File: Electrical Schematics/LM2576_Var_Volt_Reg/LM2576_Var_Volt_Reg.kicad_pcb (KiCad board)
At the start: 2 copper layers, 4 parts, among them J1 Conn_01x03_Pin, U1 LM2576S-12

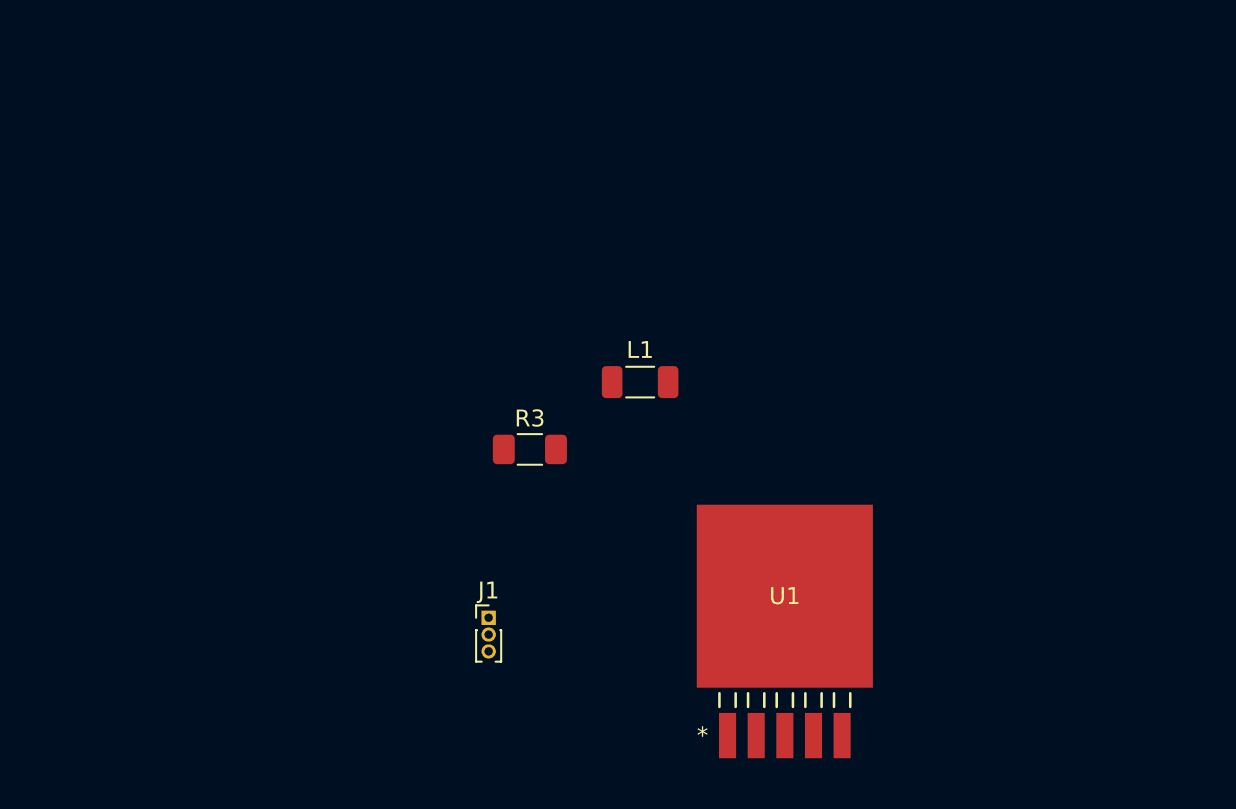
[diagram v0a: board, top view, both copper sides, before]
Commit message: added lm2679
Updated LM2576 schematic and started creating PCB layout
Created LM2679 Schematic
Updated some slicer code to open config file more easily when only main is open
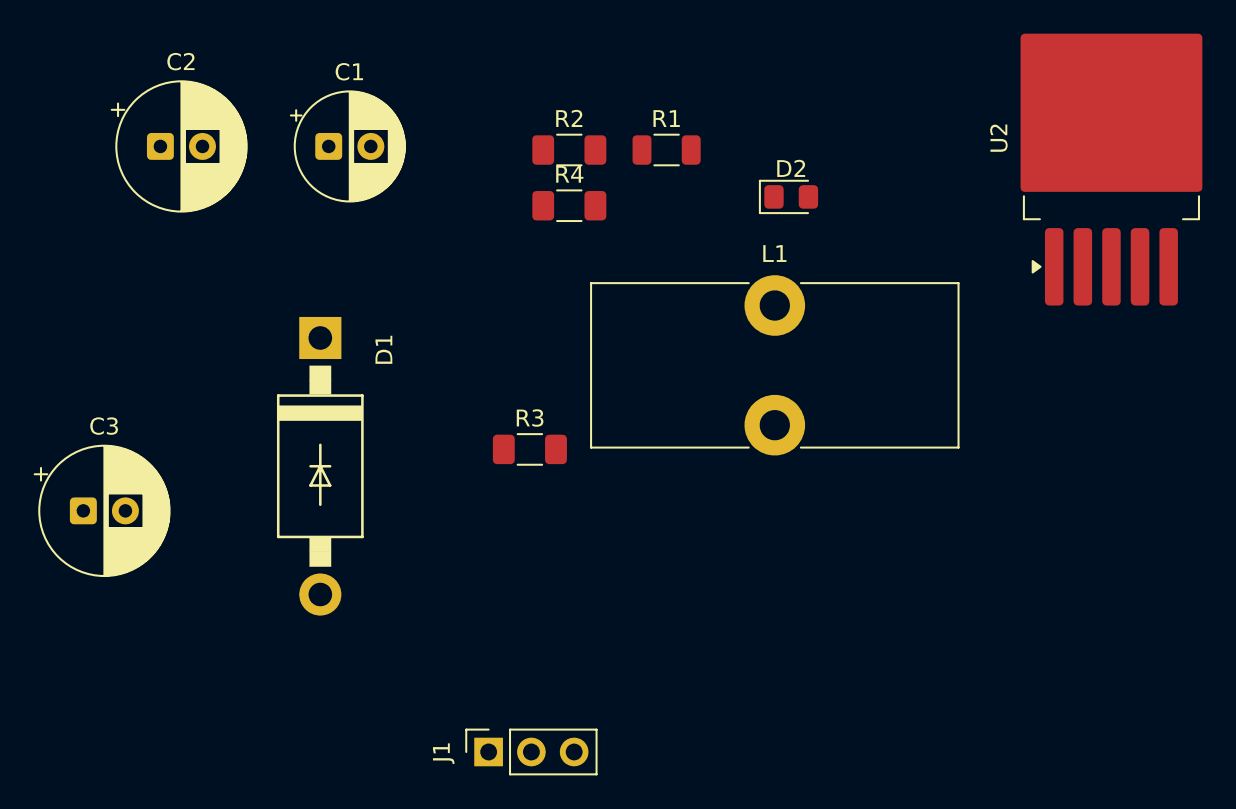
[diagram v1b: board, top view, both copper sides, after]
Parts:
- removed U1: LM2576S-12, LM2576:TS5B_TEX
- added C1: 100uF, Capacitor_THT:CP_Radial_D6.3mm_P2.50mm, F.Cu at (86.5, 32.0)
- added C2: 470uF, Capacitor_THT:CP_Radial_D7.5mm_P2.50mm, F.Cu at (76.5, 32.0)
- added C3: 470uF, Capacitor_THT:CP_Radial_D7.5mm_P2.50mm, F.Cu at (71.9, 53.6)
- added D1: MBR360G, MBR360:DIOAD950W125L840D505, F.Cu at (86.0, 51.0)
- added D2: LED, LED_SMD:LED_0805_2012Metric_Pad1.15x1.40mm_HandSolder, F.Cu at (114.0, 35.0)
- added R1: 1k, Resistor_SMD:R_1206_3216Metric, F.Cu at (106.6, 32.2)
- added R2: Rvar, Resistor_SMD:R_1206_3216Metric_Pad1.30x1.75mm_HandSolder, F.Cu at (100.8, 32.2)
- added R4: Ropt, Resistor_SMD:R_1206_3216Metric_Pad1.30x1.75mm_HandSolder, F.Cu at (100.8, 35.5)
- added U2: LM2576HVS-ADJ, Package_TO_SOT_SMD:TO-263-5_TabPin3, F.Cu at (133.0, 31.5)
- J1: footprint Connector_PinHeader_1.00mm:PinHeader_1x03_P1.00mm_Vertical -> Connector_PinSocket_2.54mm:PinSocket_1x03_P2.54mm_Vertical
- L1: footprint Inductor_SMD:L_1206_3216Metric_Pad1.22x1.90mm_HandSolder -> Inductor_THT:L_Toroid_Vertical_L21.6mm_W9.5mm_P7.11mm_Pulse_C
- moved L1 9.20 mm to (113.0, 41.5)
- moved J1 7.97 mm to (96.0, 68.0), turned to 90 degrees
